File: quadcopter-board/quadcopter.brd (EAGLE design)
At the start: 113 x 113 mm, 77 parts, among them J2 AVR_SPI_PRG_6NS, SW1 PUSHBUTTON_SMD-VERTICAL-1, U2 ATMEGA128RFA1

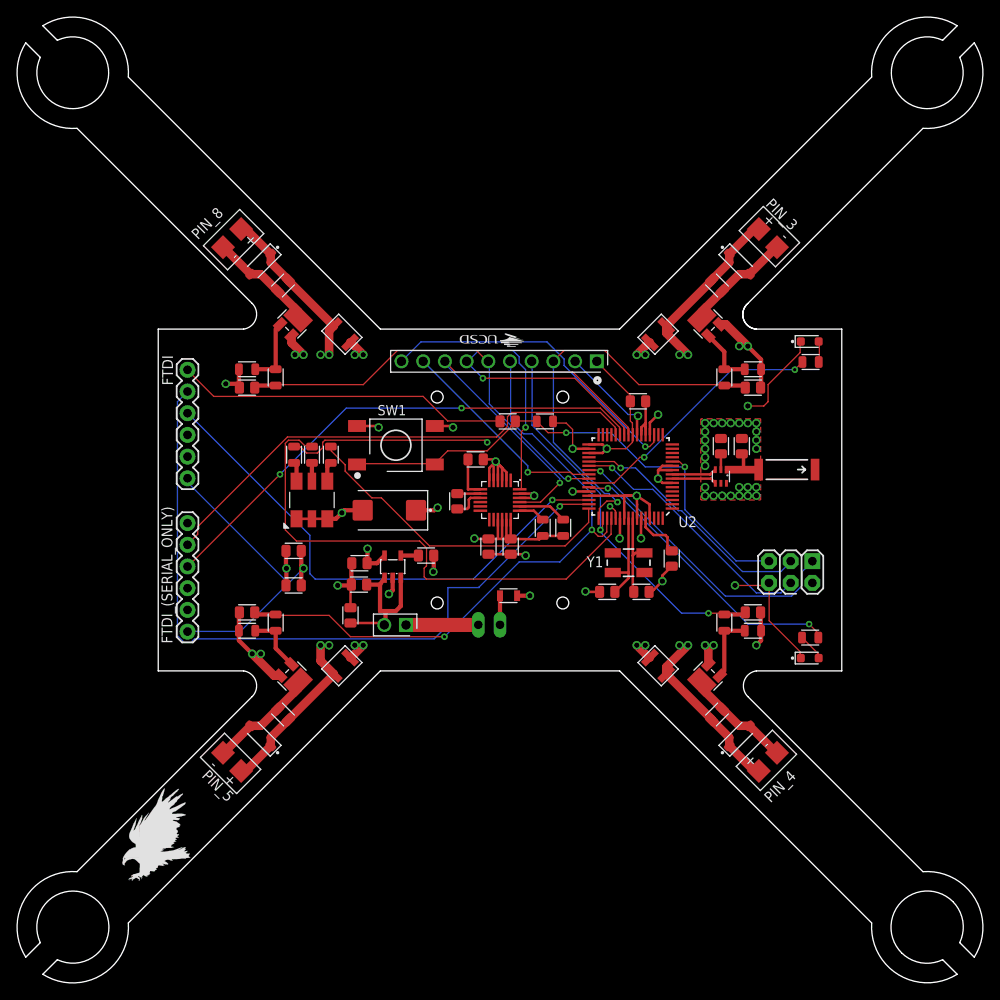
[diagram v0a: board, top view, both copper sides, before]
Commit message: Applied update to library and dru files. Passing DFM testing
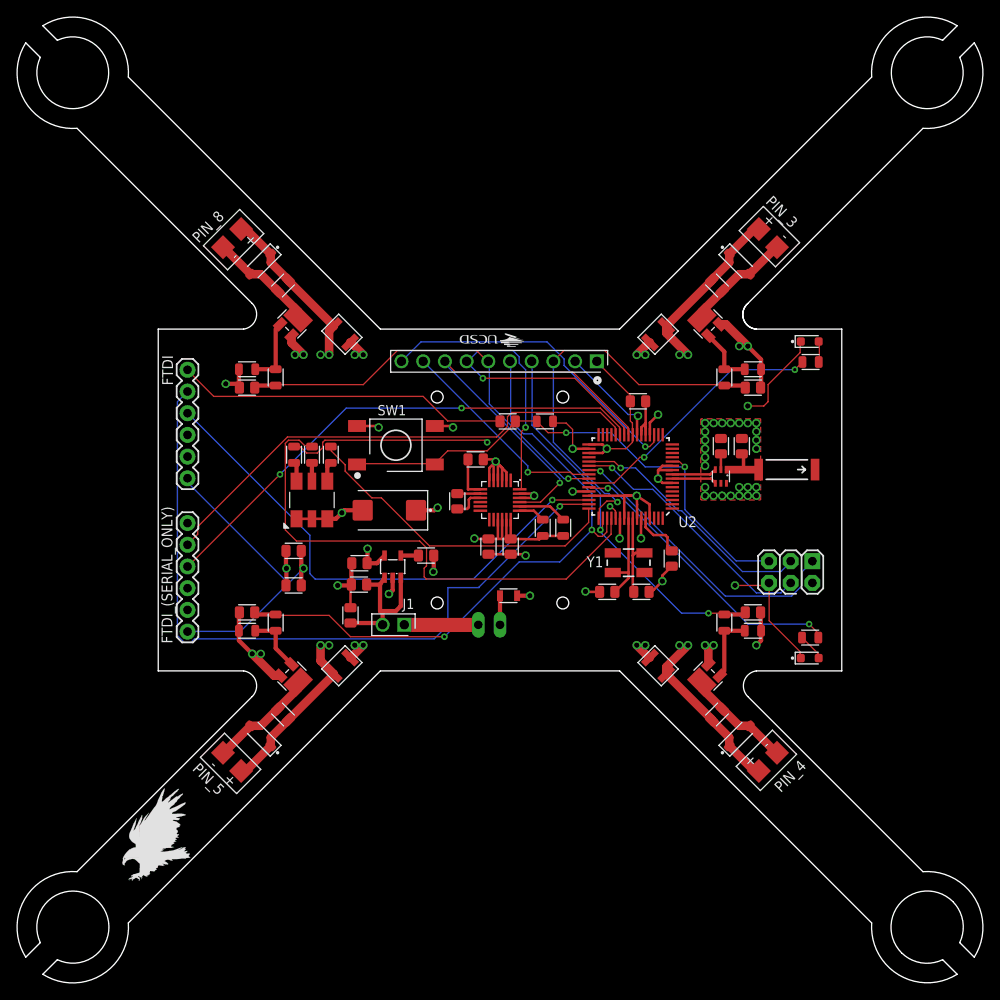
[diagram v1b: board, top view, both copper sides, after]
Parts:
- removed J4: (no value), quadparts:MALE_HEADER_2X1_0.1IN
- added J1: (no value), quadparts-rev2:MALE_HEADER_2X1_0.1IN
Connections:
- net N$17: now also J1.1; no longer J4.1
- net VCC: now also J1.2; no longer J4.2
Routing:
- added copper zone on layer 15, net N$26
- added copper zone on layer 2, net N$26
